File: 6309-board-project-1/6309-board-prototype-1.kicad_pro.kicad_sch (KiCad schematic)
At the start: 23 parts, among them J1 PWR, J2 FTDI, SW1 Reset, U1 MC6809, U2 62256, U3 28C256, U4 16550, U5 74LS04, X1 12MHz, X2 1.8432MHz, X3 24MHz, X4 1.8432MHz

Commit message: organization
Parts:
- removed X3: 24MHz, Oscillator:Oscillator_DIP-8, symbol Oscillator:CXO_DIP8
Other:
- note added: "10/24/24"
- note added: "6309 Board Prototype #1"
- note removed: "10/14/24"
- note removed: "6809 Board Prototype 1"
- note removed: "USE CANS FOR LOWER COMPONENT COUNT? VERY CHEAP"
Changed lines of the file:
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@@
-		)
-	)
-	(text "USE CANS FOR LOWER\nCOMPONENT COUNT? \nVERY CHEAP"
-		(exclude_from_sim no)
-		(at 179.07 139.7 0)
-		(effects
-			(font
-				(size 1.27 1.27)
-			)
 		)
 	)
@@
 		)
 	)
-	(text "6809 Board Prototype 1"
+	(text "6309 Board Prototype #1"
 		(exclude_from_sim no)
 		(at 198.882 189.992 0)
@@
 		)
 	)
-	(text "10/14/24\n"
+	(text "10/24/24\n"
 		(exclude_from_sim no)
 		(at 211.836 193.548 0)
@@
 					(unit 1)
 				)
-			)
-		)
-	)
-	(symbol
-		(lib_id "Oscillator:CXO_DIP8")
-		(at 158.75 154.94 0)
-		(unit 1)
-		(exclude_from_sim no)
-		(in_bom yes)
-		(on_board yes)
-		(dnp no)
-		(fields_autoplaced yes)
-		(property "Reference" "X3"
-			(at 168.91 148.6214 0)
-			(effects
-				(font
-					(size 1.27 1.27)
-				)
-			)
-		)
-		(property "Value" "24MHz"
-			(at 168.91 151.1614 0)
-			(effects
-				(font
-					(size 1.27 1.27)
-				)
-			)
-		)
-		(property "Footprint" "Oscillator:Oscillator_DIP-8"
-			(at 170.18 163.83 0)
-			(effects
-				(font
-					(size 1.27 1.27)
-				)
-				(hide yes)
-			)
-		)
-		(property "Datasheet" "http://cdn-reichelt.de/documents/datenblatt/B400/OSZI.pdf"
-			(at 156.21 154.94 0)
-			(effects
-				(font
-					(size 1.27 1.27)
-				)
-				(hide yes)
-			)
-		)
-		(property "Description" "Crystal Clock Oscillator, DIP8-style metal package"
-			(at 158.75 154.94 0)
-			(effects
-				(font
-					(size 1.27 1.27)
-				)
-				(hide yes)
-			)
-		)
-		(pin "5"
-		)
-		(pin "4"
-		)
-		(pin "8"
-		)
-		(pin "1"
-		)
-		(instances
-			(project ""
-				(path "/73f02399-4449-4d3e-bf52-6d1b4c7a62b4"
-					(reference "X3")
-					(unit 1)
-				)

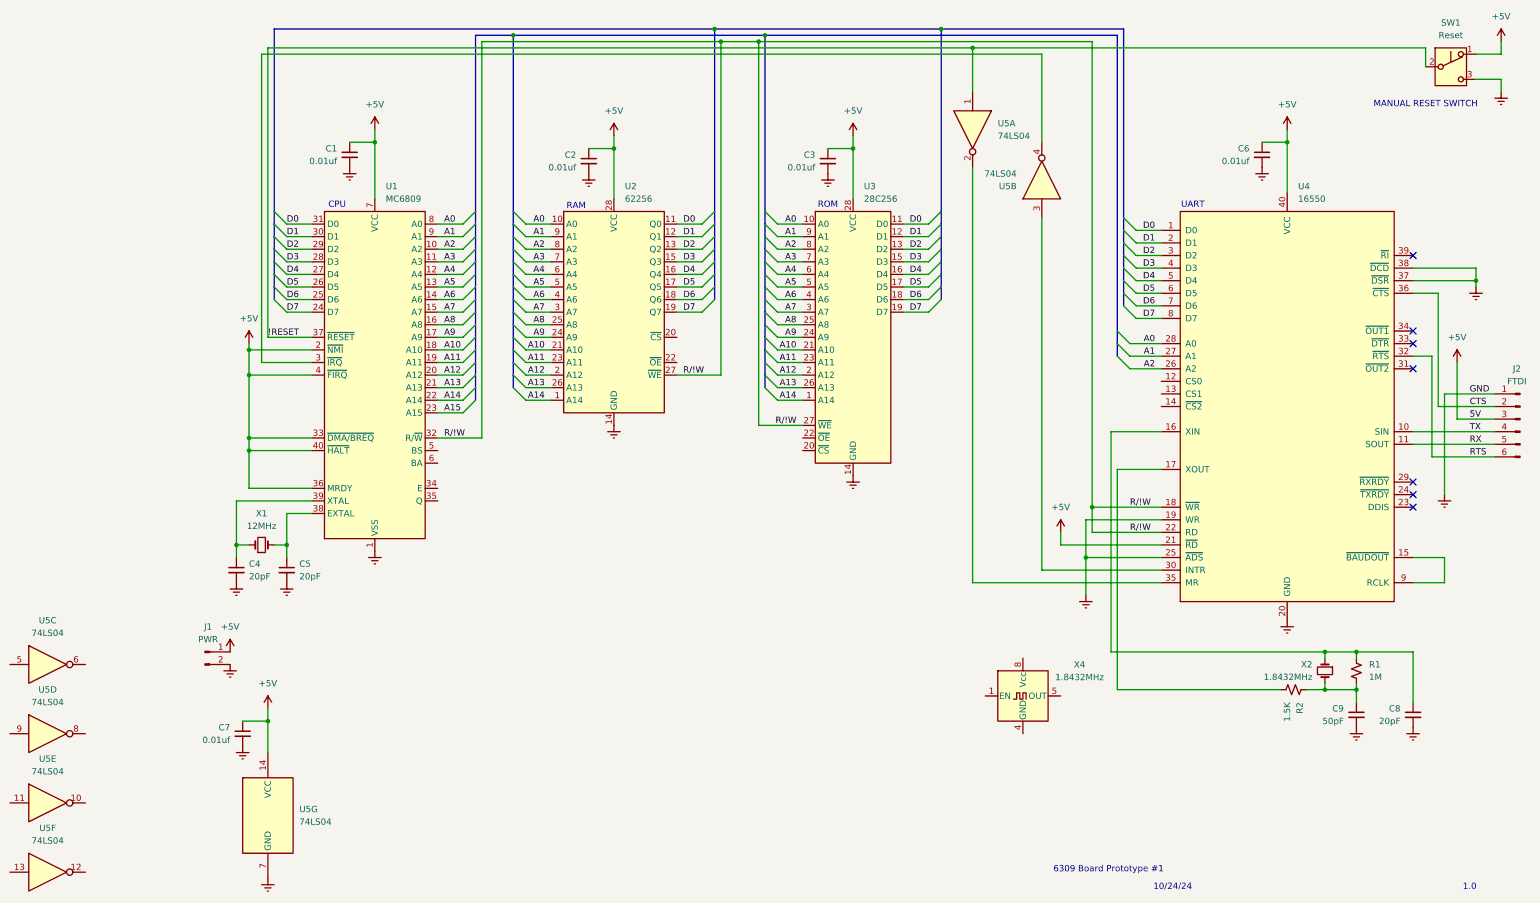
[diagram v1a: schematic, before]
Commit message: clocks on sch, 6809 datasheet, jameco xtals
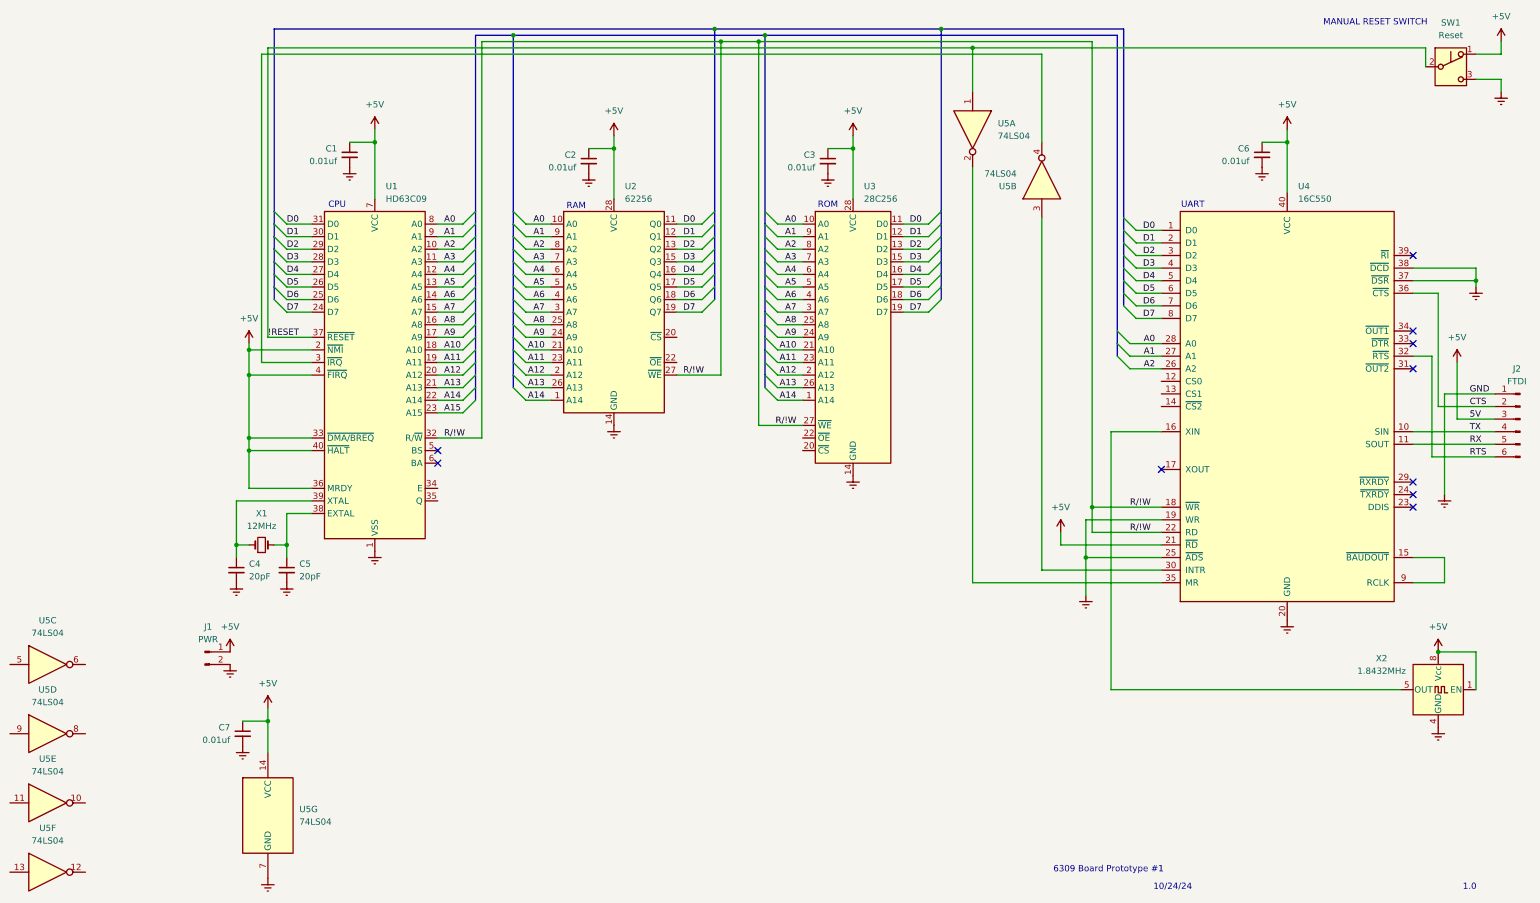
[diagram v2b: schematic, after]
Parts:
- removed C8: 20pF, symbol Device:C_Small
- removed C9: 50pF, symbol Device:C_Small
- removed R1: 1M, symbol Device:R_Small_US
- removed R2: 1.5K, symbol Device:R_Small_US
- removed X2: 1.8432MHz, symbol Device:Crystal_Small
- U1: value MC6809 -> HD63C09
- U4: value 16550 -> 16C550
- renumbered X4 to X2
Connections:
- net +5V: now also X2.1 (EN), X2.8 (Vcc)
- net GND: now also X2.4 (GND)
- net at U4.16 (XIN): now also X2.5 (OUT)
- no-connect marks 7 -> 10
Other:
- moved on the sheet: X2
